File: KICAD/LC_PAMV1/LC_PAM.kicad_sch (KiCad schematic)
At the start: 17 parts, among them J1 Conn_01x04, J3 Conn_01x24, J4 Conn_01x24, J5 Conn_01x02, U1 teensy_Teensy4.1

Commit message: 07-08-24
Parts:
- BT1: footprint Battery:BatteryHolder_Keystone_103_1x20mm -> Connector_PinHeader_2.54mm:PinHeader_1x02_P2.54mm_Vertical
- U1: footprint Library:Teensy41 -> myLibrary:Teensy41
- U2, U4: footprint Library:preAmp2 -> myLibrary:preAmp2
- U3: footprint Library:ADC_V2 -> myLibrary:ADC_V2
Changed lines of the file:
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@@
 			)
 		)
-		(property "Footprint" "Battery:BatteryHolder_Keystone_103_1x20mm"
+		(property "Footprint" "Connector_PinHeader_2.54mm:PinHeader_1x02_P2.54mm_Vertical"
 			(at 83.82 117.856 90)
 			(effects
@@
 			)
 		)
-		(property "Footprint" "Library:preAmp2"
+		(property "Footprint" "myLibrary:preAmp2"
 			(at 74.93 90.17 0)
 			(effects
@@
 			)
 		)
-		(property "Footprint" "Library:ADC_V2"
+		(property "Footprint" "myLibrary:ADC_V2"
 			(at 121.92 87.63 0)
 			(effects
@@
 			)
 		)
-		(property "Footprint" "Library:preAmp2"
+		(property "Footprint" "myLibrary:preAmp2"
 			(at 73.66 72.39 0)
 			(effects
@@
 			)
 		)
-		(property "Footprint" "Library:Teensy41"
+		(property "Footprint" "myLibrary:Teensy41"
 			(at 209.55 96.52 0)
 			(effects

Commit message: update baseboard
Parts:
- added J2: DC/DC, Connector_PinHeader_2.54mm:PinHeader_1x03_P2.54mm_Vertical, symbol Connector_Generic:Conn_01x03
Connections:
- net GND: now also J4.15 (Pin_15), U1.34 (GND), J2.2 (Pin_2)
- net V5: now also J2.1 (Pin_1)
- net Vext: now also J2.3 (Pin_3)
- net V+: now reaches U2.3 (V+), U3.1 (V+), U4.3 (V+)
- net V-: now reaches U2.6 (V-), U3.10 (V-), U4.6 (V-)
- net VUSB: now reaches U1.49 (VUSB)
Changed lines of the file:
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@@
+		)
+	)
+	(label "V+"
+		(at 88.9 64.77 0)
+		(fields_autoplaced yes)
+		(effects
+			(font
+				(size 1.27 1.27)
+			)
+			(justify left bottom)
+		)
+	)
+	(label "V-"
+		(at 90.17 99.06 0)
+		(fields_autoplaced yes)
+		(effects
+			(font
+				(size 1.27 1.27)
+			)
+			(justify left bottom)
 		)
 	)
@@
 		)
 	)
+	(label "GND"
+		(at 38.1 139.7 0)
+		(fields_autoplaced yes)
+		(effects
+			(font
+				(size 1.27 1.27)
+			)
+			(justify left bottom)
+		)
+	)
 	(label "V3.3_EN"
 		(at 182.88 59.69 0)
@@
 		)
 	)
+	(label "VUSB"
+		(at 247.65 48.26 0)
+		(fields_autoplaced yes)
+		(effects
+			(font
+				(size 1.27 1.27)
+			)
+			(justify left bottom)
+		)
+	)
 	(label "Din"
 		(at 191.77 74.93 180)
@@
 	)
 	(label "GND"
+		(at 247.65 87.63 0)
+		(fields_autoplaced yes)
+		(effects
+			(font
+				(size 1.27 1.27)
+			)
+			(justify left bottom)
+		)
+	)
+	(label "GND"
 		(at 138.43 93.98 0)
 		(fields_autoplaced yes)
@@
 		)
 	)
+	(label "V5"
+		(at 38.1 137.16 0)
+		(fields_autoplaced yes)
+		(effects
+			(font
+				(size 1.27 1.27)
+			)
+			(justify left bottom)
+		)
+	)
 	(label "ONOFF"
 		(at 227.33 140.97 0)
+		(fields_autoplaced yes)
+		(effects
+			(font
+				(size 1.27 1.27)
+			)
+			(justify left bottom)
+		)
+	)
+	(label "Vext"
+		(at 38.1 142.24 0)
 		(fields_autoplaced yes)
 		(effects
@@
 					(unit 1)
 				)
+			)
+		)
+	)
+	(symbol
+		(lib_id "Connector_Generic:Conn_01x03")
+		(at 33.02 139.7 0)
+		(mirror y)
+		(unit 1)
+		(exclude_from_sim no)
+		(in_bom yes)
+		(on_board yes)
+		(dnp no)
+		(property "Reference" "J2"
+			(at 30.988 138.4878 0)
+			(effects
+				(font
+					(size 1.27 1.27)
+				)
+				(justify left)
+			)
+		)
+		(property "Value" "DC/DC"
+			(at 30.988 140.9121 0)
+			(effects
+				(font
+					(size 1.27 1.27)
+				)
+				(justify left)
+			)
+		)
+		(property "Footprint" "Connector_PinHeader_2.54mm:PinHeader_1x03_P2.54mm_Vertical"
+			(at 33.02 139.7 0)
+			(effects
+				(font
+					(size 1.27 1.27)
+				)
+				(hide yes)
+			)
+		)
+		(property "Datasheet" "~"
+			(at 33.02 139.7 0)
+			(effects
+				(font
+					(size 1.27 1.27)
+				)
+				(hide yes)
+			)
+		)
+		(property "Description" "Generic connector, single row, 01x03, script generated (kicad-library-utils/schlib/autogen/connector/)"
+			(at 33.02 139.7 0)
+			(effects
+				(font
+					(size 1.27 1.27)
+				)
+				(hide yes)
+			)
+		)
+		(pin "2"
+		)
+		(pin "1"
+		)
+		(pin "3"
+		)
+		(instances
+			(project ""
+				(path "/20927a42-6f96-43de-a4f5-3ee83ace2c68"
+					(reference "J2")
+					(unit 1)
+				)

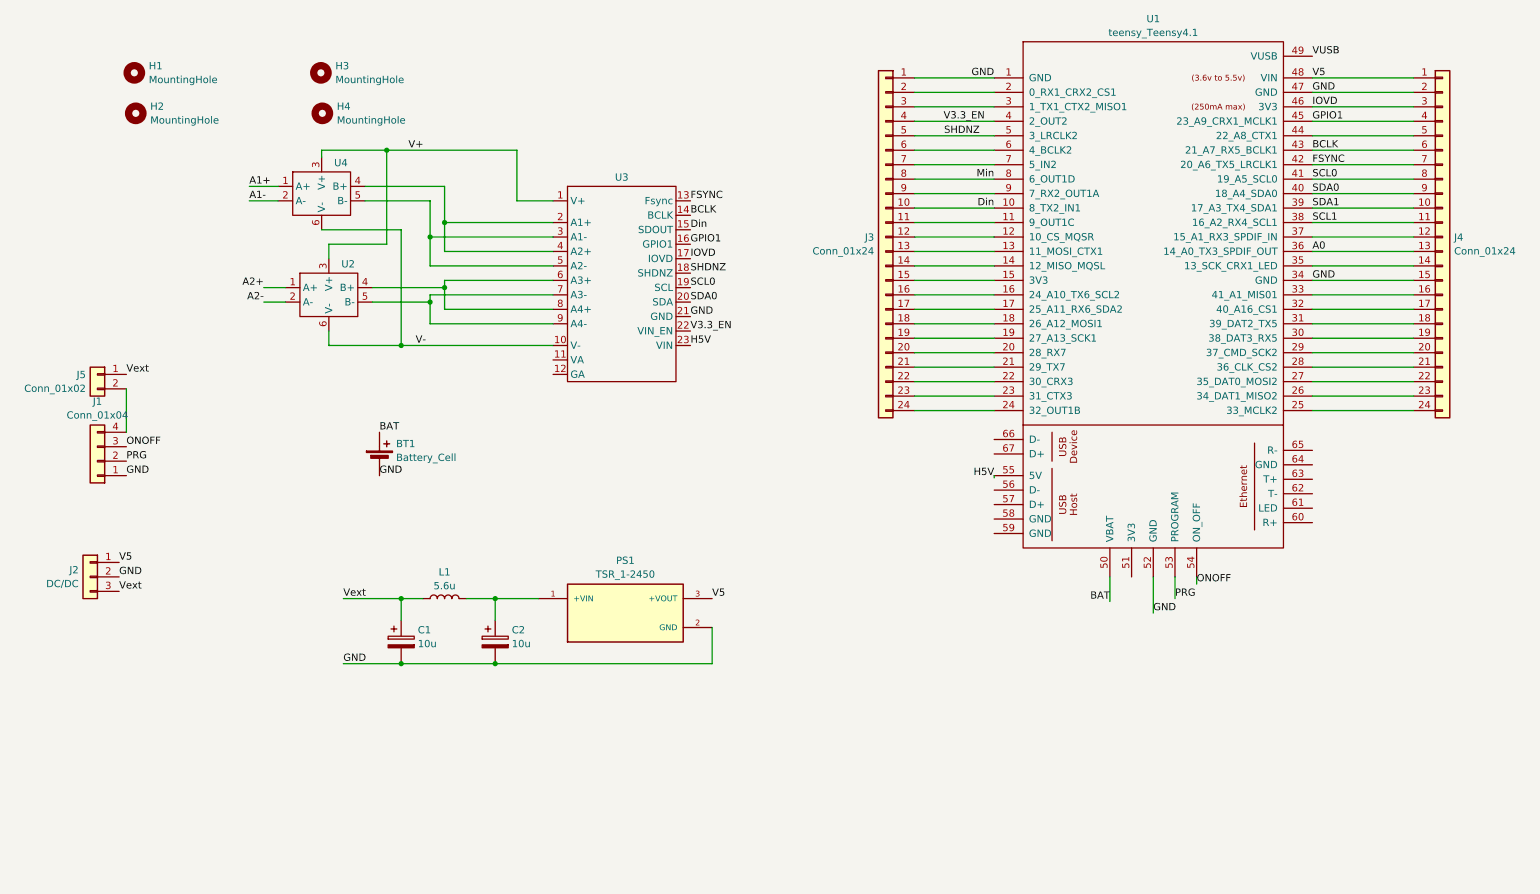
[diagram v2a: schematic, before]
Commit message: updated for fet-preamp
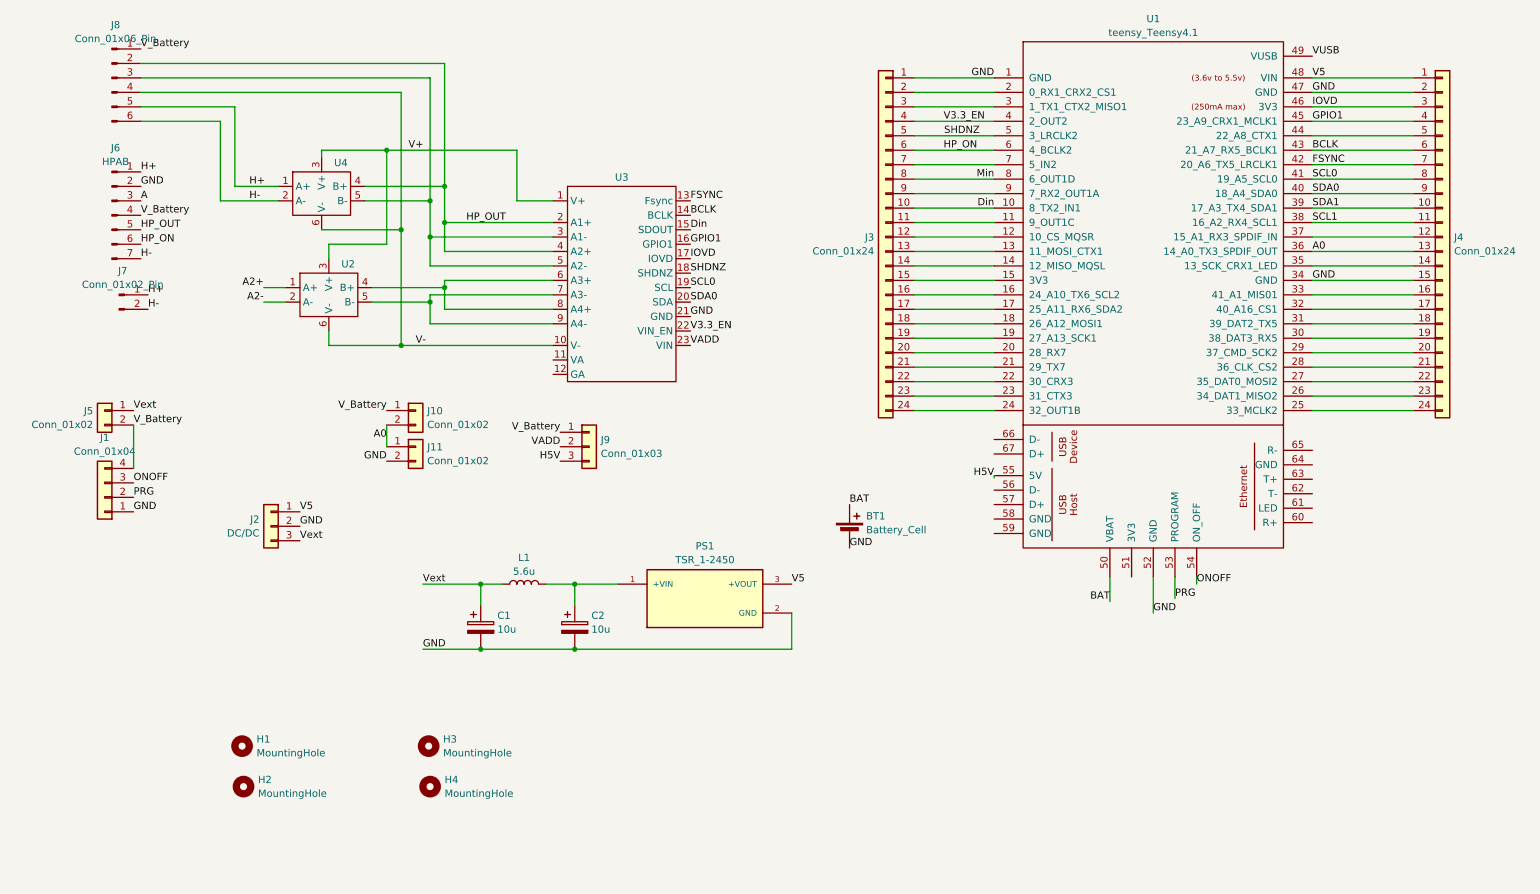
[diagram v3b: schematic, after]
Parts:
- added J10, J11: Conn_01x02, Resistor_THT:R_Axial_DIN0204_L3.6mm_D1.6mm_P1.90mm_Vertical, symbol Connector_Generic:Conn_01x02
- added J6: HPAB, myLibrary:HPAB, symbol Connector:Conn_01x07_Pin
- added J7: Conn_01x02_Pin, Connector_Molex:Molex_PicoBlade_53047-0210_1x02_P1.25mm_Vertical, symbol Connector:Conn_01x02_Pin
- added J8: Conn_01x06_Pin, myLibrary:Preamp-FET, symbol Connector:Conn_01x06_Pin
- added J9: Conn_01x03, Connector_Wire:SolderWire-0.1sqmm_1x03_P3.6mm_D0.4mm_OD1mm, symbol Connector_Generic:Conn_01x03
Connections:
- net A0: now also J10.2 (Pin_2), J11.1 (Pin_1)
- net GND: now also J11.2 (Pin_2), J6.2 (Pin_2)
- net H5V: now also J9.3 (Pin_3); no longer U3.23 (VIN)
- net V-: now also J8.4 (Pin_4)
- net HP_ON: now reaches J3.6 (Pin_6), U1.6 (4_BCLK2)
- net HP_ON: now also J6.6 (Pin_6)
- net V_Battery: now reaches J1.4 (Pin_4), J5.2 (Pin_2)
- net V_Battery: now also J10.1 (Pin_1), J6.4 (Pin_4), J8.1 (Pin_1), J9.1 (Pin_1)
- net HP_OUT: now reaches U3.2 (A1+), U3.4 (A2+), U4.4 (B+)
- net HP_OUT: now also J6.5 (Pin_5), J8.2 (Pin_2)
- net at U3.3 (A1-), U3.5 (A2-), U4.5 (B-): now also J8.3 (Pin_3)
- net A1+ renamed H+
- net H+: now also J6.1 (Pin_1), J7.1 (Pin_1), J8.5 (Pin_5)
- net A1- renamed H-
- net H-: now also J6.7 (Pin_7), J7.2 (Pin_2), J8.6 (Pin_6)
- new net A: J6.3 (Pin_3)
- new net VADD: J9.2 (Pin_2), U3.23 (VIN)
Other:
- moved on the sheet: BT1, C1, C2, H1, H2, H3, H4, J1, J2, J5, L1, PS1

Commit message: v19-12-24
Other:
- note added: "Vbat-measure"
- moved on the sheet: J10, J11, J2, J7, J9
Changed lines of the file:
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@@
 	(wire
 		(pts
-			(xy 85.09 113.03) (xy 85.09 116.84)
+			(xy 68.58 114.3) (xy 68.58 118.11)
 		)
 		(stroke
@@
 		)
 	)
+	(text "Vbat-measure"
+		(exclude_from_sim no)
+		(at 70.612 107.442 0)
+		(effects
+			(font
+				(size 1.27 1.27)
+			)
+		)
+	)
 	(label "FSYNC"
 		(at 247.65 67.31 0)
@@
 	)
 	(label "GND"
-		(at 85.09 119.38 180)
+		(at 68.58 120.65 180)
 		(fields_autoplaced yes)
 		(effects
@@
 	)
 	(label "H5V"
-		(at 115.57 119.38 180)
+		(at 99.06 118.11 180)
 		(fields_autoplaced yes)
 		(effects
@@
 	)
 	(label "V_Battery"
-		(at 115.57 114.3 180)
+		(at 99.06 113.03 180)
 		(fields_autoplaced yes)
 		(effects
@@
 	)
 	(label "A0"
-		(at 85.09 115.57 180)
+		(at 68.58 116.84 180)
 		(fields_autoplaced yes)
 		(effects
@@
 	)
 	(label "V_Battery"
-		(at 85.09 110.49 180)
+		(at 68.58 111.76 180)
 		(fields_autoplaced yes)
 		(effects
@@
 	)
 	(label "GND"
-		(at 69.85 130.81 0)
+		(at 41.91 138.43 0)
 		(fields_autoplaced yes)
 		(effects
@@
 	)
 	(label "H-"
-		(at 43.18 92.71 0)
+		(at 43.18 99.06 0)
 		(fields_autoplaced yes)
 		(effects
@@
 	)
 	(label "V5"
-		(at 69.85 128.27 0)
+		(at 41.91 135.89 0)
 		(fields_autoplaced yes)
 		(effects
@@
 	)
 	(label "Vext"
-		(at 69.85 133.35 0)
+		(at 41.91 140.97 0)
 		(fields_autoplaced yes)
 		(effects
@@
 	)
 	(label "H+"
-		(at 43.18 90.17 0)
+		(at 43.18 96.52 0)
 		(fields_autoplaced yes)
 		(effects
@@
 	)
 	(label "VADD"
-		(at 115.57 116.84 180)
+		(at 99.06 115.57 180)
 		(fields_autoplaced yes)
 		(effects
@@
 	(symbol
 		(lib_id "Connector_Generic:Conn_01x02")
-		(at 90.17 116.84 0)
+		(at 73.66 118.11 0)
 		(unit 1)
 		(exclude_from_sim no)
@@
 		(fields_autoplaced yes)
 		(property "Reference" "J11"
-			(at 92.202 116.8978 0)
+			(at 75.692 118.1678 0)
 			(effects
 				(font
@@
 		)
 		(property "Value" "Conn_01x02"
-			(at 92.202 119.3221 0)
+			(at 75.692 120.5921 0)
 			(effects
 				(font
@@
 		)
 		(property "Footprint" "Resistor_THT:R_Axial_DIN0204_L3.6mm_D1.6mm_P1.90mm_Vertical"
-			(at 90.17 116.84 0)
+			(at 73.66 118.11 0)
 			(effects
 				(font
@@
 		)
 		(property "Datasheet" "~"
-			(at 90.17 116.84 0)
+			(at 73.66 118.11 0)
 			(effects
 				(font
@@
 		)
 		(property "Description" "Generic connector, single row, 01x02, script generated (kicad-library-utils/schlib/autogen/connector/)"
-			(at 90.17 116.84 0)
+			(at 73.66 118.11 0)
 			(effects
 				(font
@@
 	(symbol
 		(lib_id "Connector_Generic:Conn_01x03")
-		(at 64.77 130.81 0)
+		(at 36.83 138.43 0)
 		(mirror y)
 		(unit 1)
@@
 		(dnp no)
 		(property "Reference" "J2"
-			(at 62.738 129.5978 0)
+			(at 34.798 137.2178 0)
 			(effects
 				(font
@@
 		)
 		(property "Value" "DC/DC"
-			(at 62.738 132.0221 0)
+			(at 34.798 139.6421 0)
 			(effects
 				(font
@@
 		)
 		(property "Footprint" "Connector_PinHeader_2.54mm:PinHeader_1x03_P2.54mm_Vertical"
-			(at 64.77 130.81 0)
+			(at 36.83 138.43 0)
 			(effects
 				(font
@@
 		)
 		(property "Datasheet" "~"
-			(at 64.77 130.81 0)
+			(at 36.83 138.43 0)
 			(effects
 				(font
@@
 		)
 		(property "Description" "Generic connector, single row, 01x03, script generated (kicad-library-utils/schlib/autogen/connector/)"
-			(at 64.77 130.81 0)
+			(at 36.83 138.43 0)
 			(effects
 				(font
@@
 	(symbol
 		(lib_id "Connector:Conn_01x02_Pin")
-		(at 38.1 90.17 0)
+		(at 38.1 96.52 0)
 		(unit 1)
 		(exclude_from_sim no)
@@
 		(fields_autoplaced yes)
 		(property "Reference" "J7"
-			(at 38.735 85.9493 0)
+			(at 38.735 92.2993 0)
 			(effects
 				(font
@@
 		)
 		(property "Value" "Conn_01x02_Pin"
-			(at 38.735 88.3736 0)
+			(at 38.735 94.7236 0)
 			(effects
 				(font
@@
 		)
 		(property "Footprint" "Connector_Molex:Molex_PicoBlade_53047-0210_1x02_P1.25mm_Vertical"
-			(at 38.1 90.17 0)
+			(at 38.1 96.52 0)
 			(effects
 				(font
@@
 		)
 		(property "Datasheet" "~"
-			(at 38.1 90.17 0)
+			(at 38.1 96.52 0)
 			(effects
 				(font
@@
 		)
 		(property "Description" "Generic connector, single row, 01x02, script generated"
-			(at 38.1 90.17 0)
+			(at 38.1 96.52 0)
 			(effects
 				(font
@@
 	(symbol
 		(lib_id "Connector_Generic:Conn_01x03")
-		(at 120.65 116.84 0)
+		(at 104.14 115.57 0)
 		(unit 1)
 		(exclude_from_sim no)
@@
 		(fields_autoplaced yes)
 		(property "Reference" "J9"
-			(at 122.682 115.6278 0)
+			(at 106.172 114.3578 0)
 			(effects
 				(font
@@
 		)
 		(property "Value" "Conn_01x03"
-			(at 122.682 118.0521 0)
+			(at 106.172 116.7821 0)
 			(effects
 				(font
@@
 		)
 		(property "Footprint" "Connector_Wire:SolderWire-0.1sqmm_1x03_P3.6mm_D0.4mm_OD1mm"
-			(at 120.65 116.84 0)
+			(at 104.14 115.57 0)
 			(effects
 				(font
@@
 		)
 		(property "Datasheet" "~"
-			(at 120.65 116.84 0)
+			(at 104.14 115.57 0)
 			(effects
 				(font
@@
 		)
 		(property "Description" "Generic connector, single row, 01x03, script generated (kicad-library-utils/schlib/autogen/connector/)"
-			(at 120.65 116.84 0)
+			(at 104.14 115.57 0)
 			(effects
 				(font
@@
 	(symbol
 		(lib_id "Connector_Generic:Conn_01x02")
-		(at 90.17 110.49 0)
+		(at 73.66 111.76 0)
 		(unit 1)
 		(exclude_from_sim no)
@@
 		(fields_autoplaced yes)
 		(property "Reference" "J10"
-			(at 92.202 110.5478 0)
+			(at 75.692 111.8178 0)
 			(effects
 				(font
@@
 		)
 		(property "Value" "Conn_01x02"
-			(at 92.202 112.9721 0)
+			(at 75.692 114.2421 0)
 			(effects
 				(font
@@
 		)
 		(property "Footprint" "Resistor_THT:R_Axial_DIN0204_L3.6mm_D1.6mm_P1.90mm_Vertical"
-			(at 90.17 110.49 0)
+			(at 73.66 111.76 0)
 			(effects
 				(font
@@
 		)
 		(property "Datasheet" "~"
-			(at 90.17 110.49 0)
+			(at 73.66 111.76 0)
 			(effects
 				(font
@@
 		)
 		(property "Description" "Generic connector, single row, 01x02, script generated (kicad-library-utils/schlib/autogen/connector/)"
-			(at 90.17 110.49 0)
+			(at 73.66 111.76 0)
 			(effects
 				(font
